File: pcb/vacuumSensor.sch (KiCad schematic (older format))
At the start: 12 parts, among them J1 Conn_01x03_Male, U1 MPXA6115A, U2 MCP6022

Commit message: visual changes
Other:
- note added: "Reproduces this design: https://makr.zone/vacuum-sensor/192/"
- moved on the sheet: C1, J1, R1, R2, R3, R4, R5, R6, U1, U2A, U2B, U2C

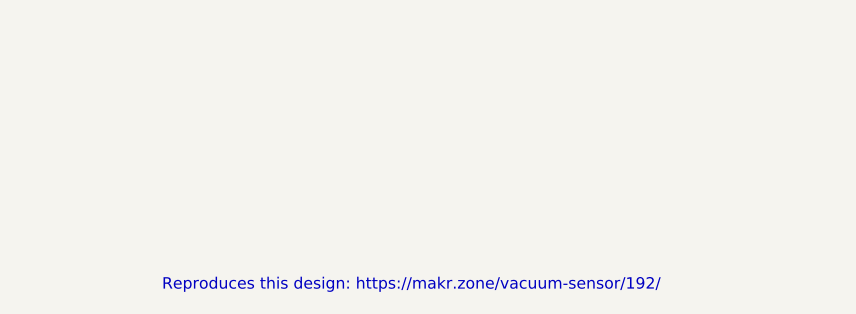
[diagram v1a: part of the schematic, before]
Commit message: Added text info to schematic.
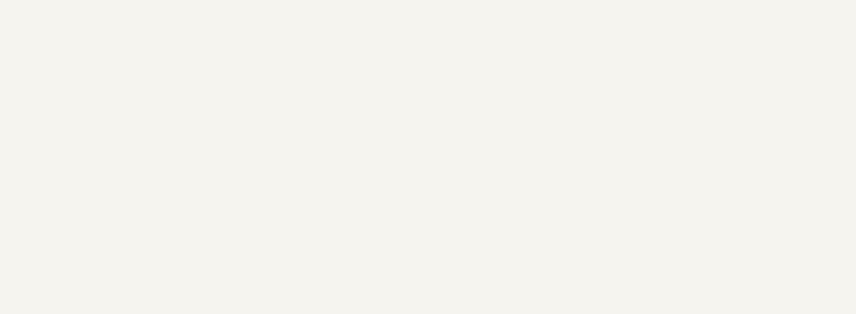
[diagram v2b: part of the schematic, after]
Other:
- note removed: "Reproduces this design: https://makr.zone/vacuum-sensor/192/"
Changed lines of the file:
@@
 Rev "1.0"
 Comp ""
-Comment1 ""
-Comment2 ""
+Comment1 "www.juliendevillers.com"
+Comment2 "https://github.com/JulienDevillers/vacuumSensorPCB"
 Comment3 ""
-Comment4 ""
+Comment4 "Reproduces this design: https://makr.zone/vacuum-sensor/192/"
 $EndDescr
 $Comp
@@
 $EndComp
 Connection ~ 3250 4550
-Text Notes 8450 6350 0    50   ~ 0
-Reproduces this design: https://makr.zone/vacuum-sensor/192/
 $EndSCHEMATC
